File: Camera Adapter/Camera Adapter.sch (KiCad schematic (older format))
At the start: 11 parts, among them J1 Conn_02x15_Top_Bottom, J2 634108150321, J3 Conn_01x02, J4 Conn_01x03, J5 Conn_02x15_Top_Bottom, J6 634108150321, U1 MC33269D-3.3G

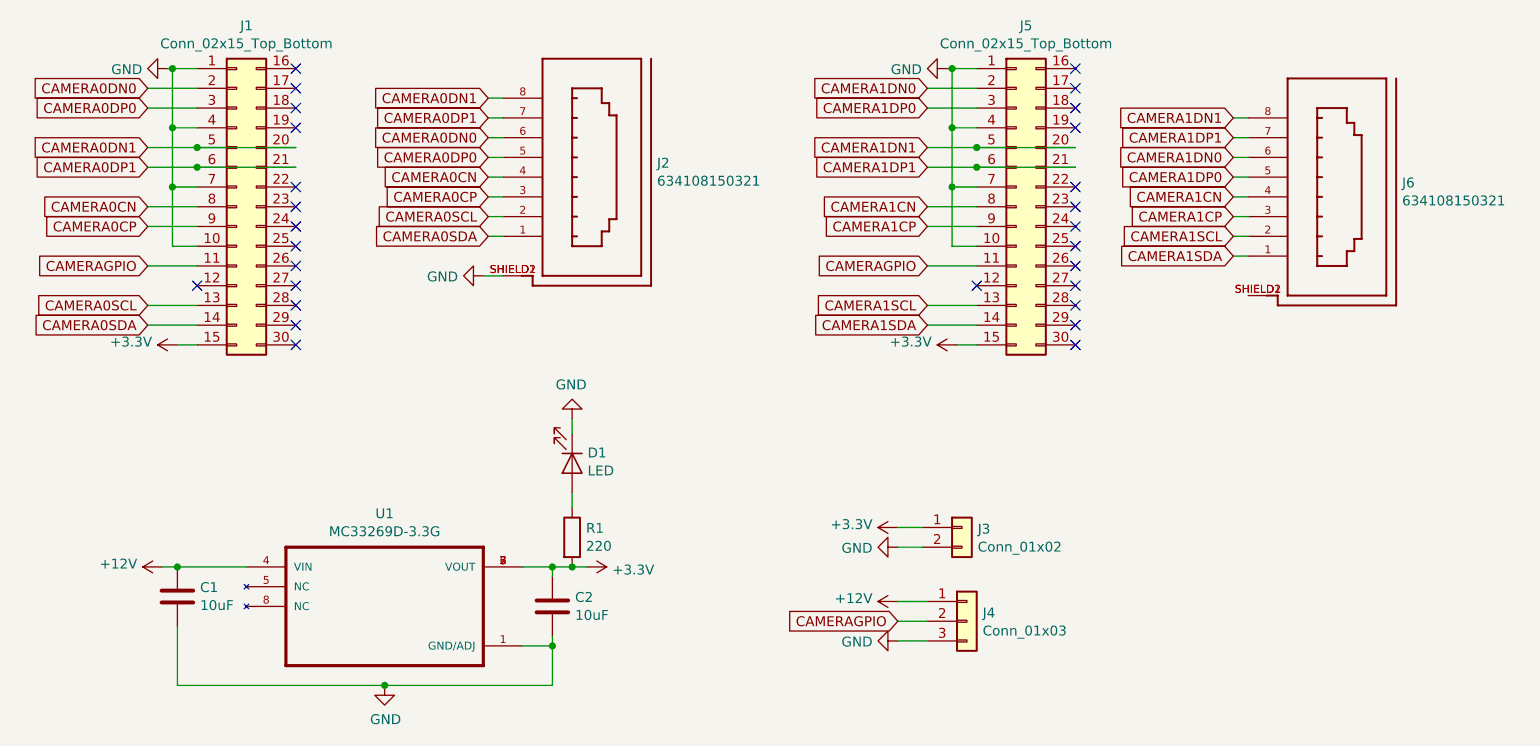
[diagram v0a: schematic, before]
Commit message: Change to different ZIF connector
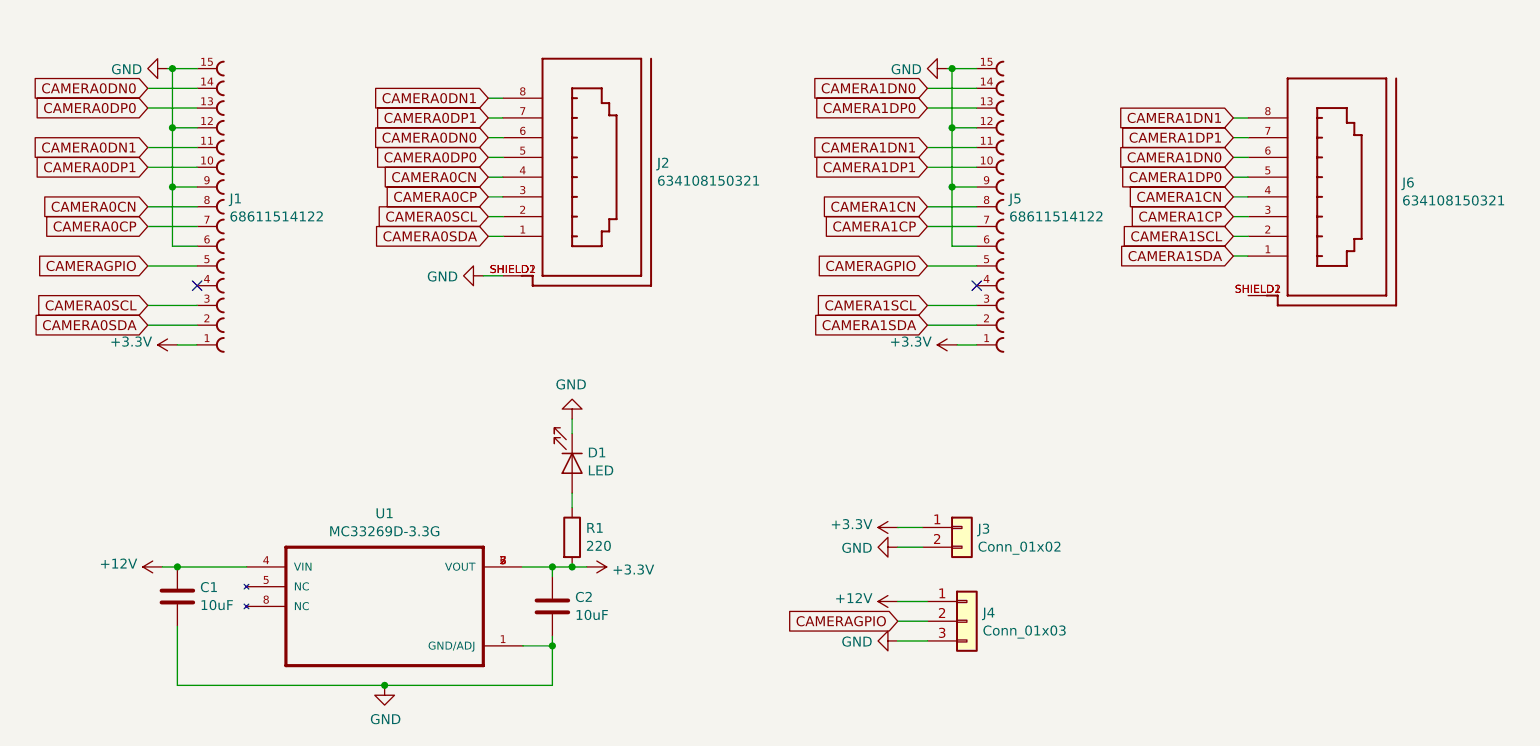
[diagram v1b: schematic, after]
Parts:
- removed J1, J5: Conn_02x15_Top_Bottom, digikey-footprints:117342485, symbol Connector_Generic:Conn_02x15_Top_Bottom
- added J1, J5: 68611514122, digikey-footprints:68611514122, symbol 68611514122:68611514122
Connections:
- net +3V3: now also J1.1 (15), J5.1 (15)
- net CAMERA0CN: now also J1.8
- net CAMERA0CP: now also J1.7 (9)
- net CAMERA0DN0: now also J1.14 (2)
- net CAMERA0DN1: now also J1.11 (5)
- net CAMERA0DP0: now also J1.13 (3)
- net CAMERA0DP1: now also J1.10 (6)
- net CAMERA0SCL: now also J1.3 (13)
- net CAMERA0SDA: now also J1.2 (14)
- net CAMERA1CN: now also J5.8
- net CAMERA1CP: now also J5.7 (9)
- net CAMERA1DN0: now also J5.14 (2)
- net CAMERA1DN1: now also J5.11 (5)
- net CAMERA1DP0: now also J5.13 (3)
- net CAMERA1DP1: now also J5.10 (6)
- net CAMERA1SCL: now also J5.3 (13)
- net CAMERA1SDA: now also J5.2 (14)
- net CAMERAGPIO: now also J1.5 (11), J5.5 (11)
- net GND: now also J1.12 (4), J1.15 (1), J1.6 (10), J1.9 (7), J5.12 (4), J5.15 (1), J5.6 (10), J5.9 (7)
- no-connect marks 28 -> 2
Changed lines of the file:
@@
 EESchema Schematic File Version 4
+LIBS:Camera Adapter-cache
 EELAYER 29 0
 EELAYER END
@@
 Comment4 ""
 $EndDescr
-$Comp
-L Connector_Generic:Conn_02x15_Top_Bottom J1
-U 1 1 5E85BBBC
-P 2125 2150
-F 0 "J1" H 2175 3067 50  0000 C CNN
-F 1 "Conn_02x15_Top_Bottom" H 2175 2976 50  0000 C CNN
-F 2 "digikey-footprints:117342485" H 2125 2150 50  0001 C CNN
-F 3 "~" H 2125 2150 50  0001 C CNN
-	1    2125 2150
-	1    0    0    -1
-$EndComp
-$Comp
-L Connector_Generic:Conn_02x15_Top_Bottom J5
-U 1 1 5E85D897
-P 6075 2150
-F 0 "J5" H 6125 3067 50  0000 C CNN
-F 1 "Conn_02x15_Top_Bottom" H 6125 2976 50  0000 C CNN
-F 2 "digikey-footprints:117342485" H 6075 2150 50  0001 C CNN
-F 3 "~" H 6075 2150 50  0001 C CNN
-	1    6075 2150
-	1    0    0    -1
-$EndComp
 $Comp
 L MC33269D-3.3G:MC33269D-3.3G U1
@@
 	1925 1650 1675 1650
 Wire Wire Line
-	1675 1850 1925 1850
-Wire Wire Line
-	1925 1950 1675 1950
-Wire Wire Line
 	1675 2150 1925 2150
 Wire Wire Line
@@
 	5875 1650 5625 1650
 Wire Wire Line
-	5625 1850 5875 1850
-Wire Wire Line
-	5875 1950 5625 1950
-Wire Wire Line
 	5625 2150 5875 2150
 Wire Wire Line
@@
 	3825 3600 3825 3675
 Wire Wire Line
-	6375 1950 5875 1950
-Connection ~ 5875 1950
-Wire Wire Line
-	6375 1850 5875 1850
-Connection ~ 5875 1850
-Wire Wire Line
-	1925 1850 2425 1850
-Connection ~ 1925 1850
-Wire Wire Line
-	2425 1950 1925 1950
-Connection ~ 1925 1950
-NoConn ~ 2425 1450
-NoConn ~ 2425 1550
-NoConn ~ 2425 1650
-NoConn ~ 2425 1750
-NoConn ~ 2425 2050
-NoConn ~ 2425 2150
-NoConn ~ 2425 2250
-NoConn ~ 2425 2350
-NoConn ~ 2425 2450
-NoConn ~ 2425 2550
-NoConn ~ 2425 2650
-NoConn ~ 2425 2750
-NoConn ~ 2425 2850
-NoConn ~ 6375 2850
-NoConn ~ 6375 2750
-NoConn ~ 6375 2650
-NoConn ~ 6375 2550
-NoConn ~ 6375 2450
-NoConn ~ 6375 2350
-NoConn ~ 6375 2250
-NoConn ~ 6375 2150
-NoConn ~ 6375 2050
-NoConn ~ 6375 1750
-NoConn ~ 6375 1650
-NoConn ~ 6375 1550
-NoConn ~ 6375 1450
+	1925 1850 1675 1850
+Wire Wire Line
+	1675 1950 1925 1950
+$Comp
+L 68611514122:68611514122 J1
+U 1 1 6366E004
+P 2125 2150
+F 0 "J1" H 2089 2190 50  0000 L CNN
+F 1 "68611514122" H 2089 2099 50  0000 L CNN
+F 2 "digikey-footprints:68611514122" H 2125 2150 50  0001 L BNN
+F 3 "" H 2125 2150 50  0001 L BNN
+F 4 "68611514122" H 2125 2150 50  0001 L BNN "Field4"
+F 5 "None" H 2125 2150 50  0001 L BNN "Field5"
+F 6 "Unavailable" H 2125 2150 50  0001 L BNN "Field6"
+F 7 "Connector [Würth Elektronik] 68611514122 Connector" H 2125 2150 50  0001 L BNN "Field7"
+F 8 "Würth Elektronik" H 2125 2150 50  0001 L BNN "Field8"
+	1    2125 2150
+	1    0    0    -1
+$EndComp
+$Comp
+L 68611514122:68611514122 J5
+U 1 1 6367193C
+P 6075 2150
+F 0 "J5" H 6039 2190 50  0000 L CNN
+F 1 "68611514122" H 6039 2099 50  0000 L CNN
+F 2 "digikey-footprints:68611514122" H 6075 2150 50  0001 L BNN
+F 3 "" H 6075 2150 50  0001 L BNN
+F 4 "68611514122" H 6075 2150 50  0001 L BNN "Field4"
+F 5 "None" H 6075 2150 50  0001 L BNN "Field5"
+F 6 "Unavailable" H 6075 2150 50  0001 L BNN "Field6"
+F 7 "Connector [Würth Elektronik] 68611514122 Connector" H 6075 2150 50  0001 L BNN "Field7"
+F 8 "Würth Elektronik" H 6075 2150 50  0001 L BNN "Field8"
+	1    6075 2150
+	1    0    0    -1
+$EndComp
+Wire Wire Line
+	5625 1850 5875 1850
+Wire Wire Line
+	5875 1950 5625 1950
 $EndSCHEMATC

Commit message: Updated KiCad files
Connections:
- net GND: now also J6.SHIELD1 (SHIELD), J6.SHIELD2 (SHIELD)
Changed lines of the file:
@@
 Wire Wire Line
 	5875 1950 5625 1950
+$Comp
+L power:GND #PWR0114
+U 1 1 64014CD3
+P 7200 2600
+F 0 "#PWR0114" H 7200 2350 50  0001 C CNN
+F 1 "GND" V 7205 2472 50  0000 R CNN
+F 2 "" H 7200 2600 50  0001 C CNN
+F 3 "" H 7200 2600 50  0001 C CNN
+	1    7200 2600
+	0    1    1    0
+$EndComp
+Wire Wire Line
+	7200 2600 7250 2600
 $EndSCHEMATC
